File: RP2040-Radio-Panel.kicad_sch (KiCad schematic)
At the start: 3 parts

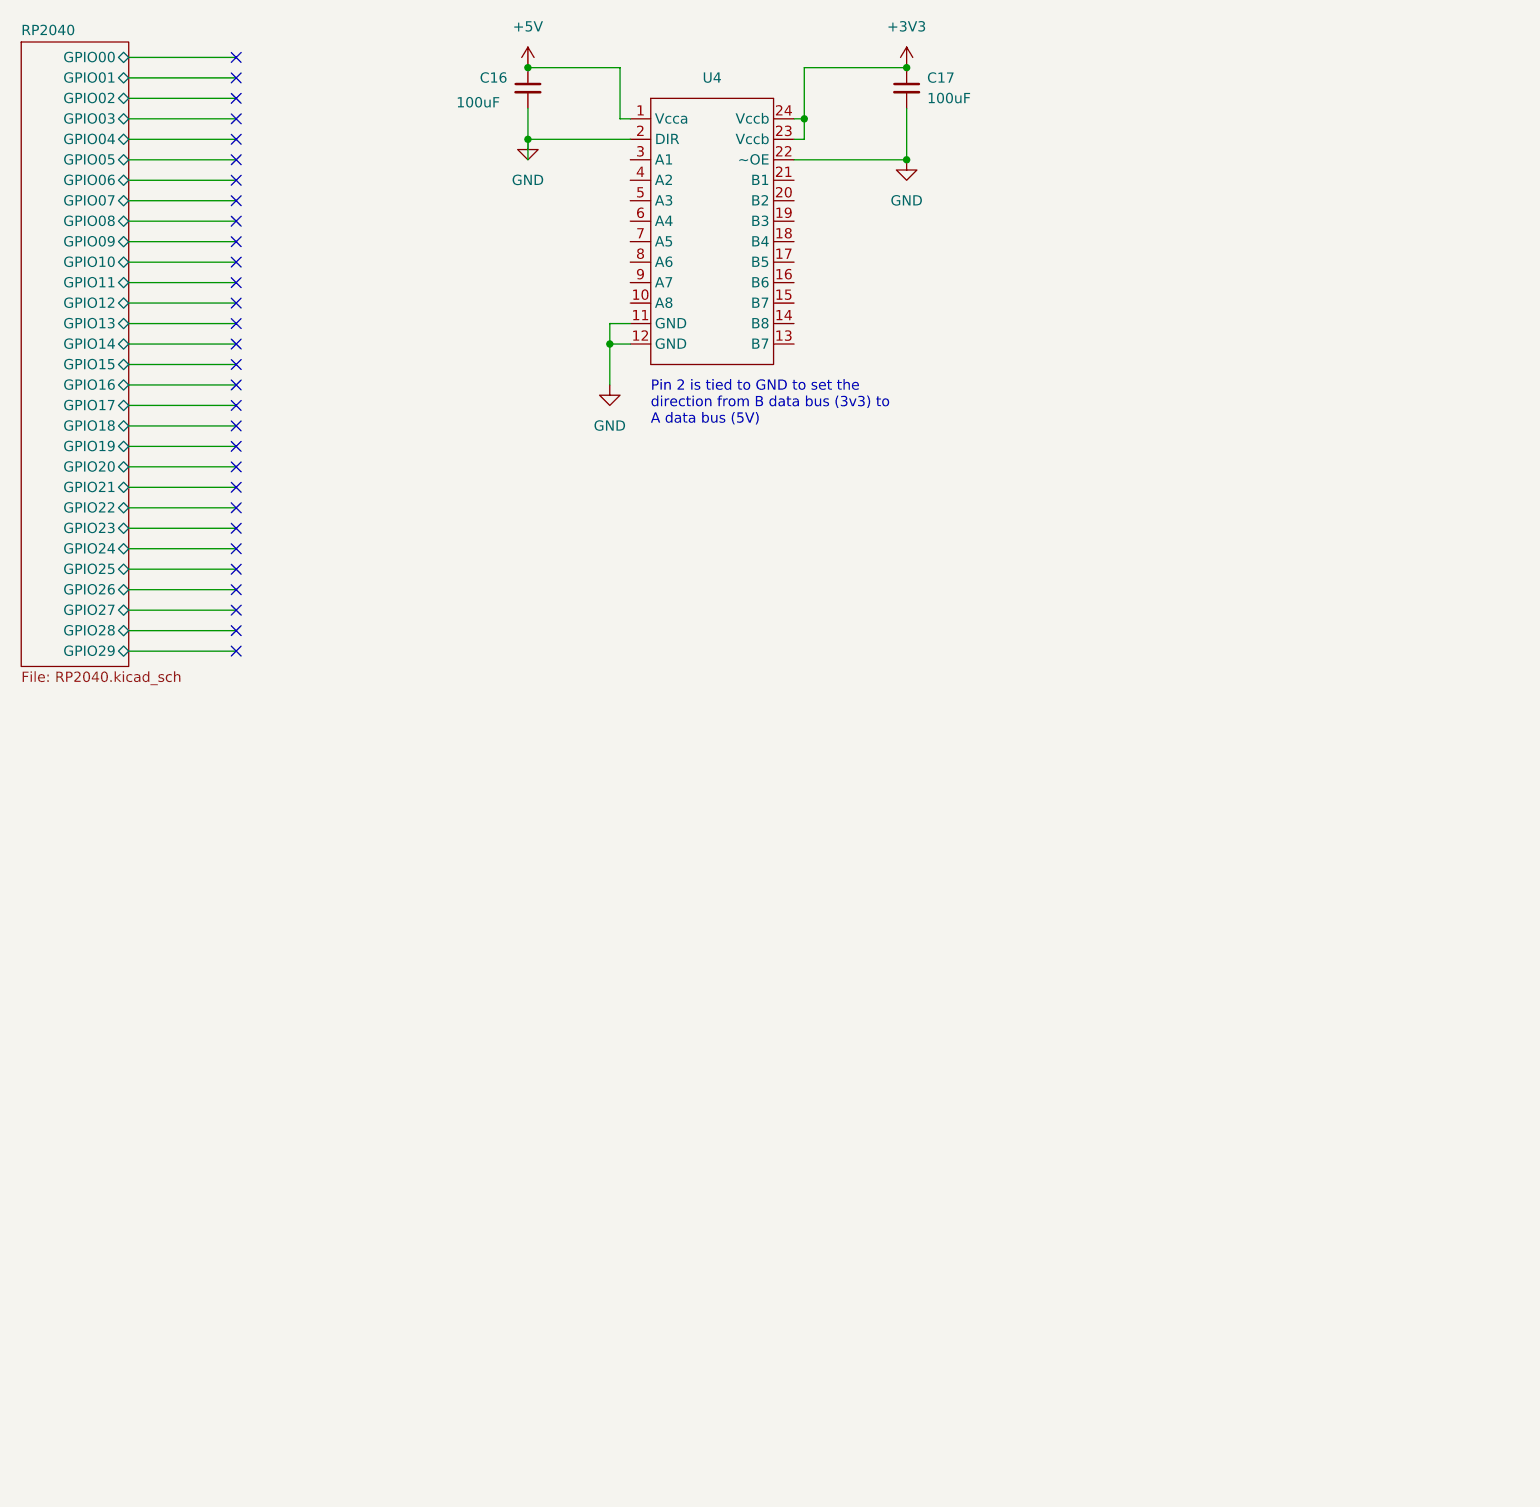
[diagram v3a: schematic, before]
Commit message: Add some displays
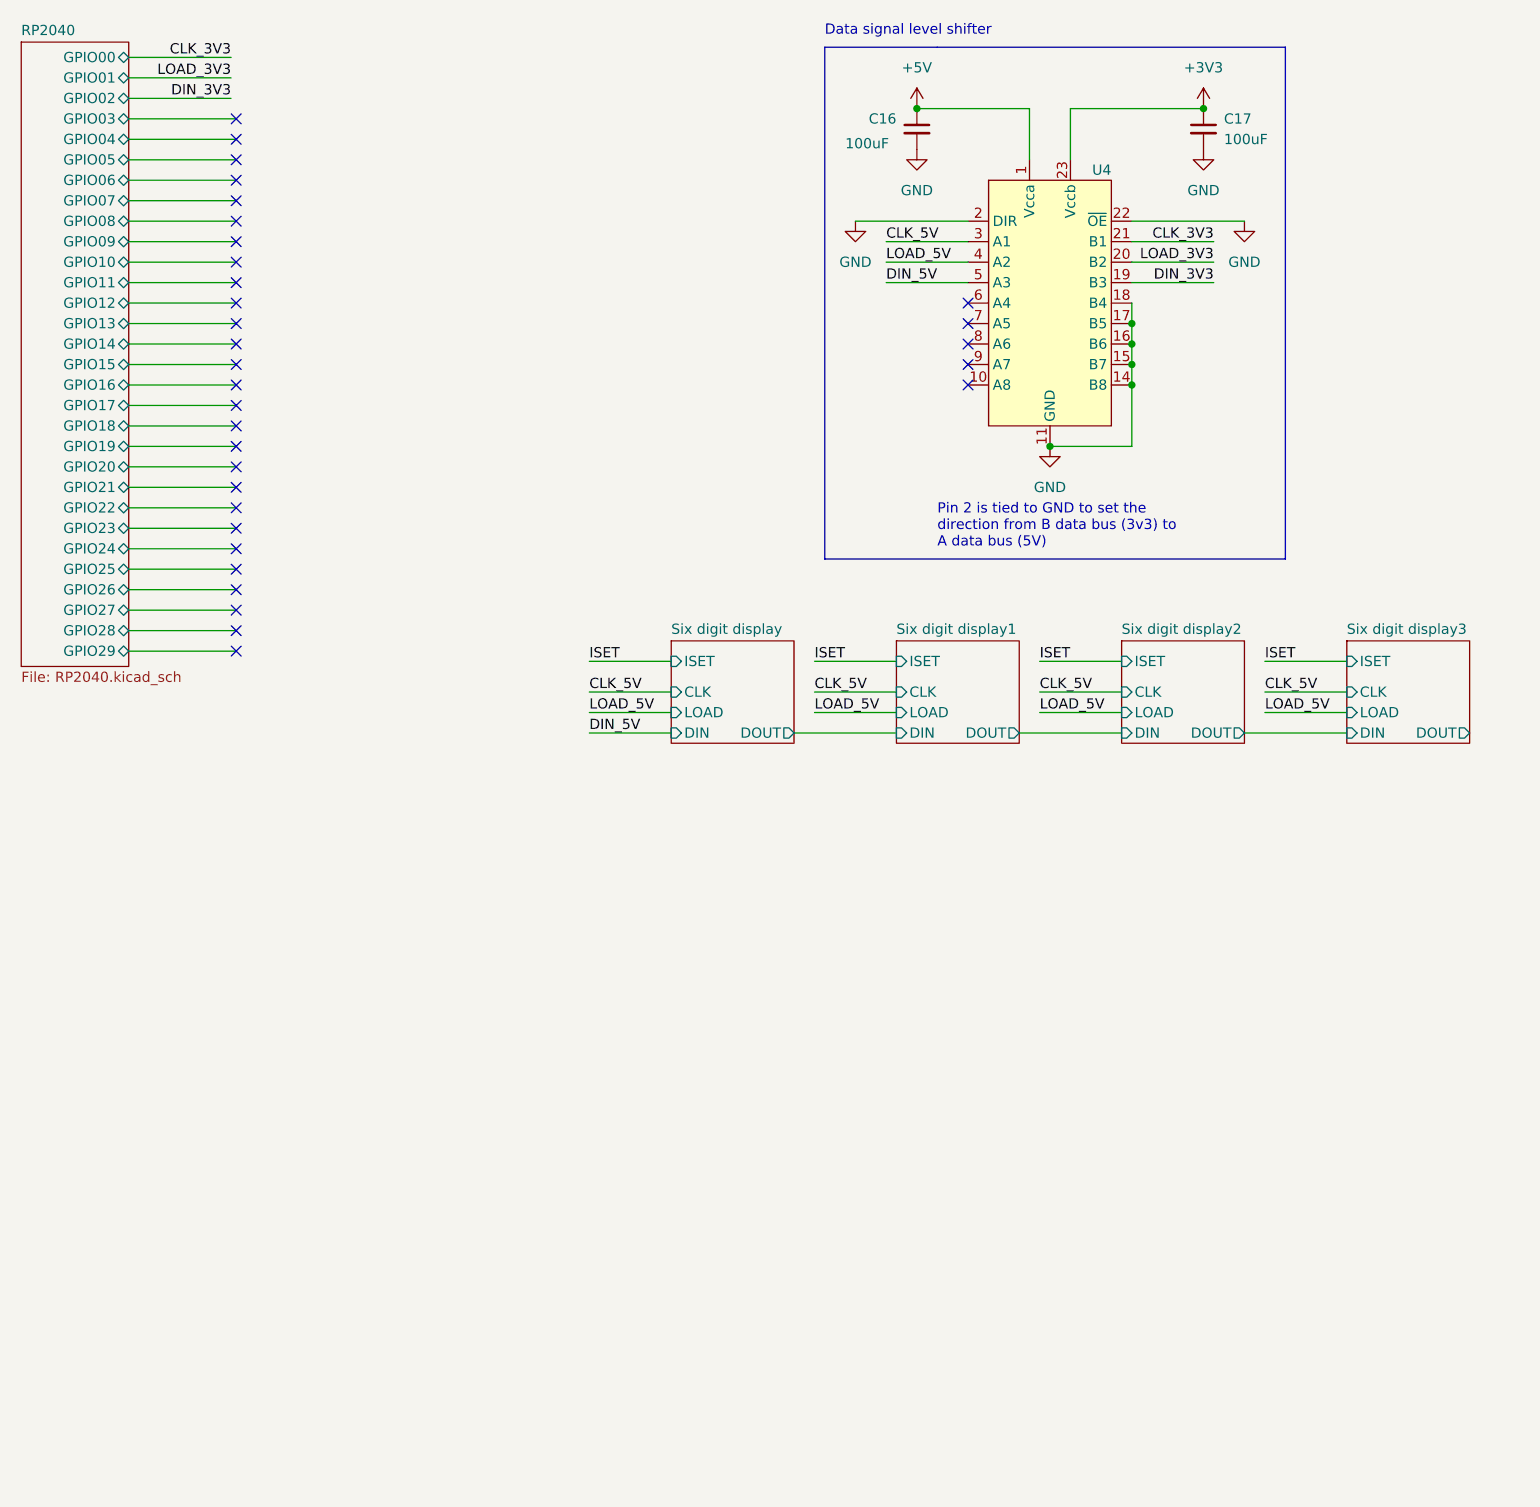
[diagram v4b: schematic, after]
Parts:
- removed U4: ~, Package_SO:TSSOP-24_4.4x7.8mm_P0.65mm, symbol Custom_Symbols:SN74LVC4245APWR
- added U4: SN74LVC4245APWR, Package_SO:TSSOP-24_4.4x7.8mm_P0.65mm, symbol SimPanel:SN74LVC4245APWR
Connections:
- net +3V3: now also U4.23 (Vccb), U4.24 (Vccb)
- net +5V: now also U4.1 (Vcca)
- net GND: now also U4.11 (GND), U4.12 (GND), U4.13 (GND), U4.14 (B8), U4.15 (B7), U4.16 (B6), U4.17 (B5), U4.18 (B4), U4.2 (DIR), U4.22 (~{OE})
- new net CLK_3V3: U4.21 (B1)
- new net CLK_5V: U4.3 (A1)
- new net DIN_3V3: U4.19 (B3)
- new net DIN_5V: U4.5 (A3)
- new net LOAD_3V3: U4.20 (B2)
- new net LOAD_5V: U4.4 (A2)
- no-connect marks 30 -> 32
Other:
- added sheet Six digit display (sixDigitDisplay.kicad_sch)
- added sheet Six digit display1 (sixDigitDisplay.kicad_sch)
- added sheet Six digit display2 (sixDigitDisplay.kicad_sch)
- added sheet Six digit display3 (sixDigitDisplay.kicad_sch)
- note added: "Data signal level shifter"
- moved on the sheet: C16, C17

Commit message: More layout
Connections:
- no-connect marks 32 -> 6
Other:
- added sheet Six digit display4 (sixDigitDisplay.kicad_sch)
- added sheet Six digit display5 (sixDigitDisplay.kicad_sch)
- added sheet Six digit display6 (sixDigitDisplay.kicad_sch)
- added sheet Six digit display7 (sixDigitDisplay.kicad_sch)
- sheet RP2040 ports: added I2C0_SCL, I2C0_SDA; removed GPIO00, GPIO01
- note added: "Frequency 1 active/standby"
- note added: "Frequency 2 active/standby"
- note added: "Frequency 3 active/standby"
- note added: "Frequency 4 active/standby"
- note added: "Seven segment displays"

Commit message: Update footprints
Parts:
- C16, C17: footprint (none) -> Custom_Footprints:Perfect_0402
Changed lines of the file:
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@@
+    )
+  )
+  (symbol (lib_id "power:GND") (at 161.29 30.48 0) (unit 1)
+    (in_bom yes) (on_board yes) (dnp no) (fields_autoplaced)
+    (property "Reference" "#PWR027" (at 161.29 36.83 0)
+      (effects (font (size 1.27 1.27)) hide)
+    )
+    (property "Value" "GND" (at 161.29 35.56 0)
+      (effects (font (size 1.27 1.27)))
+    )
+    (property "Footprint" "" (at 161.29 30.48 0)
+      (effects (font (size 1.27 1.27)) hide)
+    )
+    (property "Datasheet" "" (at 161.29 30.48 0)
+      (effects (font (size 1.27 1.27)) hide)
+    )
+    (pin "1")
+    (instances
+      (project "RP2040-Radio-Panel"
+        (path "/e63e39d7-6ac0-4ffd-8aa3-1841a4541b55"
+          (reference "#PWR027") (unit 1)
+        )
+      )
     )
   )
@@
       (effects (font (size 1.27 1.27)) (justify left))
     )
-    (property "Footprint" "" (at 161.29 27.94 0)
+    (property "Footprint" "Custom_Footprints:Perfect_0402" (at 161.29 27.94 0)
       (effects (font (size 1.27 1.27)) hide)
     )
@@
       (effects (font (size 1.27 1.27)) (justify left bottom))
     )
-    (property "Footprint" "" (at 125.73 27.94 0)
+    (property "Footprint" "Custom_Footprints:Perfect_0402" (at 125.73 27.94 0)
       (effects (font (size 1.27 1.27)) hide)
     )
@@
         )
       )
-    )
-  )
-  (symbol (lib_id "power:GND") (at 161.29 30.48 0) (unit 1)
-    (in_bom yes) (on_board yes) (dnp no) (fields_autoplaced)
-    (property "Reference" "C16" (at 161.29 36.83 0)
-      (effects (font (size 1.27 1.27)) hide)
-    )
-    (property "Value" "GND" (at 161.29 35.56 0)
-      (effects (font (size 1.27 1.27)))
-    )
-    (property "Footprint" "" (at 161.29 30.48 0)
-      (effects (font (size 1.27 1.27)) hide)
-    )
-    (property "Datasheet" "" (at 161.29 30.48 0)
-      (effects (font (size 1.27 1.27)) hide)
-    )
-    (pin "1")
-    (instances
-      (project "RP2040-Radio-Panel"
-        (path "/e63e39d7-6ac0-4ffd-8aa3-1841a4541b55"
-          (reference "C16") (unit 1)
-        )
-      )
